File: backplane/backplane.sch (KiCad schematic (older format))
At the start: 0 parts

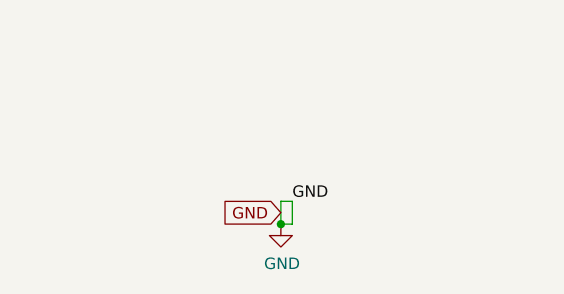
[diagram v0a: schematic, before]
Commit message: Connected GND planes using vias with common net
Added new footprint linked with net from two floating inductors in schematic
to associate both planes and all vias to connect everything together.
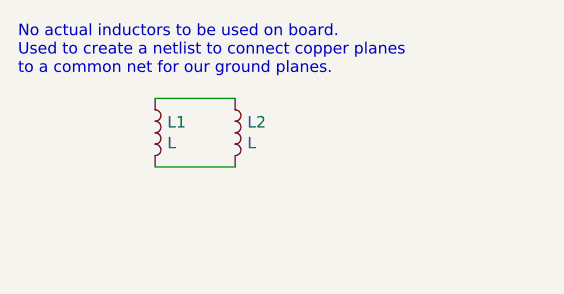
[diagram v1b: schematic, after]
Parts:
- added L1, L2: L, DxWiFi:GND-pad, symbol Device:L
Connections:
- new net: L1.1, L2.1
- new net: L1.2, L2.2
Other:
- note added: "No actual inductors to be used on board.\nUsed to create a netlist to connect copper planes \nto a common net for our ground planes."
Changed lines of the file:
@@
 $EndDescr
 $Comp
-L power:GND #PWR0101
-U 1 1 5CD9D487
-P 5550 5050
-F 0 "#PWR0101" H 5550 4800 50  0001 C CNN
-F 1 "GND" H 5555 4877 50  0000 C CNN
-F 2 "" H 5550 5050 50  0001 C CNN
-F 3 "" H 5550 5050 50  0001 C CNN
-	1    5550 5050
+L Device:L L1
+U 1 1 5CDA2A41
+P 5000 4650
+F 0 "L1" H 5053 4696 50  0000 L CNN
+F 1 "L" H 5053 4605 50  0000 L CNN
+F 2 "DxWiFi:GND-pad" H 5000 4650 50  0001 C CNN
+F 3 "~" H 5000 4650 50  0001 C CNN
+	1    5000 4650
+	1    0    0    -1
+$EndComp
+$Comp
+L Device:L L2
+U 1 1 5CDA301B
+P 5350 4650
+F 0 "L2" H 5403 4696 50  0000 L CNN
+F 1 "L" H 5403 4605 50  0000 L CNN
+F 2 "DxWiFi:GND-pad" H 5350 4650 50  0001 C CNN
+F 3 "~" H 5350 4650 50  0001 C CNN
+	1    5350 4650
 	1    0    0    -1
 $EndComp
 Wire Wire Line
-	5600 5050 5550 5050
-Connection ~ 5550 5050
+	5350 4500 5000 4500
 Wire Wire Line
-	5600 4950 5600 5050
-Wire Wire Line
-	5550 4950 5600 4950
-Wire Wire Line
-	5550 5050 5550 4950
-Text Label 5600 4950 0    50   ~ 0
-GND
-Text GLabel 5550 5000 0    50   Input ~ 0
-GND
+	5000 4800 5350 4800
+Text Notes 4400 4400 0    50   ~ 0
+No actual inductors to be used on board.\nUsed to create a netlist to connect copper planes \nto a common net for our ground planes.
 $EndSCHEMATC
